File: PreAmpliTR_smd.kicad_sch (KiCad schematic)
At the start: 30 parts, among them J1 Conn_01x02, J2 Conn_01x02, J3 Conn_01x02, Q1 Q_NPN_BEC, Q2 Q_NPN_BEC

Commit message: cambio de valores de los filtros
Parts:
- C3: value 100n -> 680p
- C4: value 100n -> 4700p
- C5: value 1n -> 470p
- C6: value 1n -> 4700p
- R6: value 3K3 -> 100k
- R7: value 3K3 -> 68k
- R8: value 6K8 -> 100k
- RV2, RV3: value 100K -> 1M
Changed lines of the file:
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@@
   (symbol (lib_id "Device:R") (at 123.825 108.585 90) (unit 1)
     (in_bom yes) (on_board yes) (dnp no) (fields_autoplaced)
-    (property "Reference" "R7" (at 123.825 103.505 90)
-      (effects (font (size 1.27 1.27)))
-    )
-    (property "Value" "3K3" (at 123.825 106.045 90)
+    (property "Reference" "R7" (at 123.825 104.14 90)
+      (effects (font (size 1.27 1.27)))
+    )
+    (property "Value" "68k" (at 123.825 106.68 90)
       (effects (font (size 1.27 1.27)))
     )
@@
   (symbol (lib_id "Device:C") (at 92.075 154.305 270) (unit 1)
     (in_bom yes) (on_board yes) (dnp no) (fields_autoplaced)
-    (property "Reference" "C5" (at 92.075 147.955 90)
-      (effects (font (size 1.27 1.27)))
-    )
-    (property "Value" "1n" (at 92.075 150.495 90)
+    (property "Reference" "C5" (at 92.075 148.59 90)
+      (effects (font (size 1.27 1.27)))
+    )
+    (property "Value" "470p" (at 92.075 151.13 90)
       (effects (font (size 1.27 1.27)))
     )
@@
   (symbol (lib_id "Device:C") (at 97.155 114.935 180) (unit 1)
     (in_bom yes) (on_board yes) (dnp no) (fields_autoplaced)
-    (property "Reference" "C3" (at 100.965 114.3 0)
+    (property "Reference" "C3" (at 100.33 114.3 0)
       (effects (font (size 1.27 1.27)) (justify right))
     )
-    (property "Value" "100n" (at 100.965 116.84 0)
+    (property "Value" "680p" (at 100.33 116.84 0)
       (effects (font (size 1.27 1.27)) (justify right))
     )
@@
   (symbol (lib_id "Device:R") (at 90.805 108.585 90) (unit 1)
     (in_bom yes) (on_board yes) (dnp no) (fields_autoplaced)
-    (property "Reference" "R6" (at 90.805 103.505 90)
-      (effects (font (size 1.27 1.27)))
-    )
-    (property "Value" "3K3" (at 90.805 106.045 90)
+    (property "Reference" "R6" (at 90.805 104.14 90)
+      (effects (font (size 1.27 1.27)))
+    )
+    (property "Value" "100k" (at 90.805 106.68 90)
       (effects (font (size 1.27 1.27)))
     )
@@
       (effects (font (size 1.27 1.27)))
     )
-    (property "Value" "100K" (at 107.315 106.045 90)
+    (property "Value" "1M" (at 107.315 106.045 90)
       (effects (font (size 1.27 1.27)))
     )
@@
   (symbol (lib_id "Device:R") (at 107.315 127.635 180) (unit 1)
     (in_bom yes) (on_board yes) (dnp no) (fields_autoplaced)
-    (property "Reference" "R8" (at 109.855 127 0)
+    (property "Reference" "R8" (at 109.22 127 0)
       (effects (font (size 1.27 1.27)) (justify right))
     )
-    (property "Value" "6K8" (at 109.855 129.54 0)
+    (property "Value" "100k" (at 109.22 129.54 0)
       (effects (font (size 1.27 1.27)) (justify right))
     )
@@
       (effects (font (size 1.27 1.27)))
     )
-    (property "Value" "100K" (at 107.315 156.845 90)
+    (property "Value" "1M" (at 107.315 156.845 90)
       (effects (font (size 1.27 1.27)))
     )
@@
   (symbol (lib_id "Device:C") (at 117.475 116.205 180) (unit 1)
     (in_bom yes) (on_board yes) (dnp no) (fields_autoplaced)
-    (property "Reference" "C4" (at 121.285 115.57 0)
+    (property "Reference" "C4" (at 120.65 115.57 0)
       (effects (font (size 1.27 1.27)) (justify right))
     )
-    (property "Value" "100n" (at 121.285 118.11 0)
+    (property "Value" "4700p" (at 120.65 118.11 0)
       (effects (font (size 1.27 1.27)) (justify right))
     )
@@
   (symbol (lib_id "Device:C") (at 121.285 154.305 270) (unit 1)
     (in_bom yes) (on_board yes) (dnp no) (fields_autoplaced)
-    (property "Reference" "C6" (at 121.285 147.955 90)
-      (effects (font (size 1.27 1.27)))
-    )
-    (property "Value" "1n" (at 121.285 150.495 90)
-      (effects (font (size 1.27 1.27)))
-    )
+    (property "Reference" "C6" (at 121.285 148.59 90)
+      (effects (font (size 1.27 1.27)))
+    )
+    (property "Value" "4700p" (at 121.285 151.13 90)
+      (effects (font (size 1.27 1.27)))
+    )

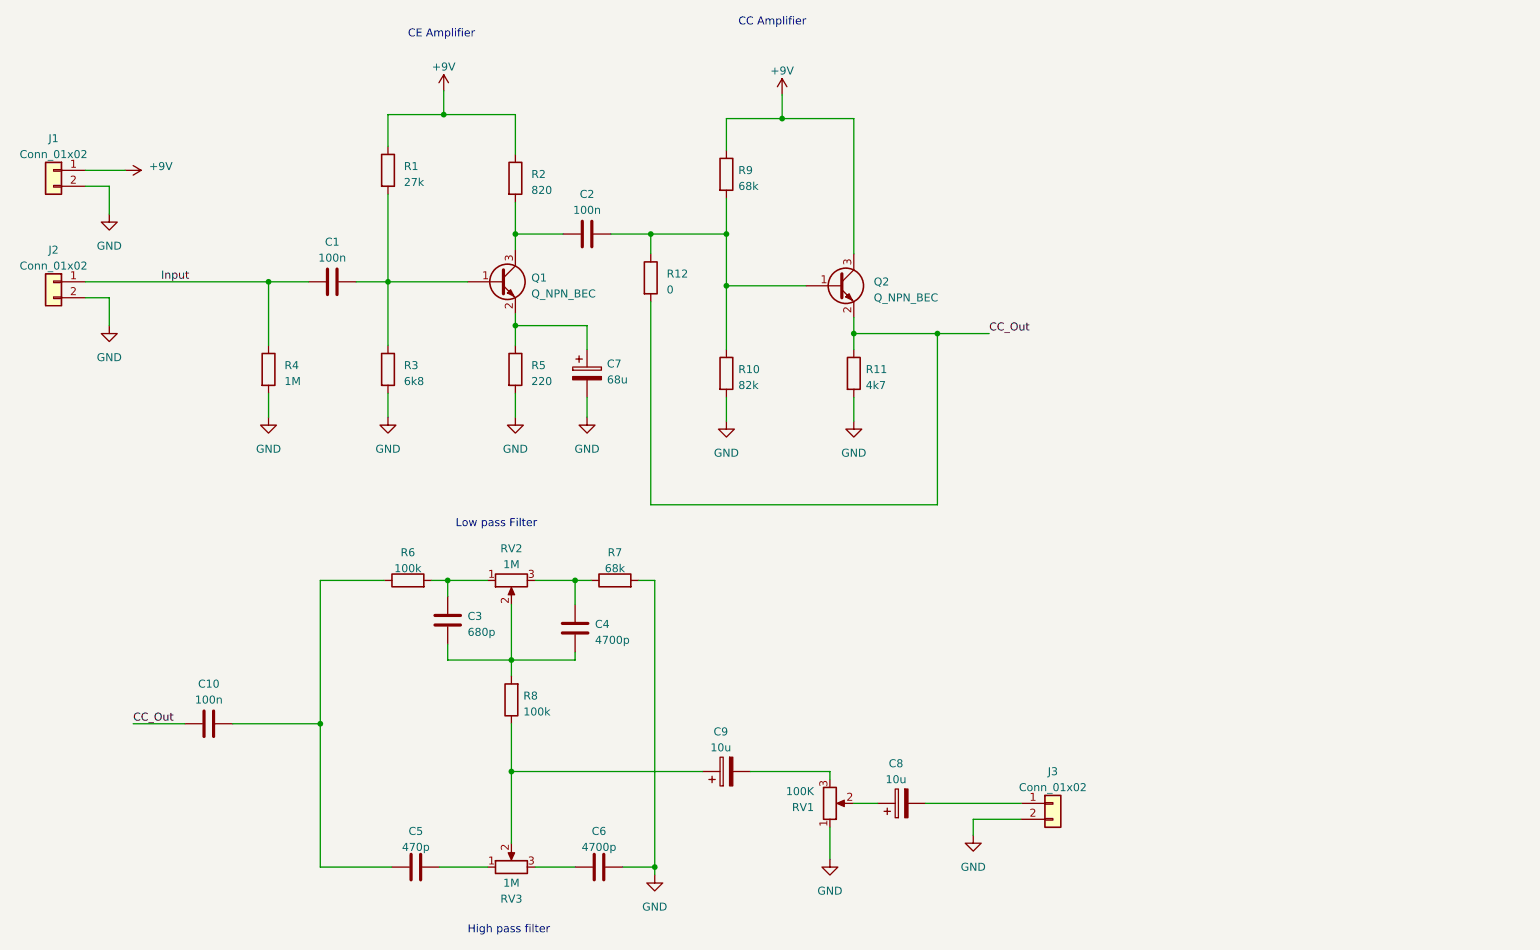
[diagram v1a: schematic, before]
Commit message: cambio de bloques: ec - filtro - cc - salida
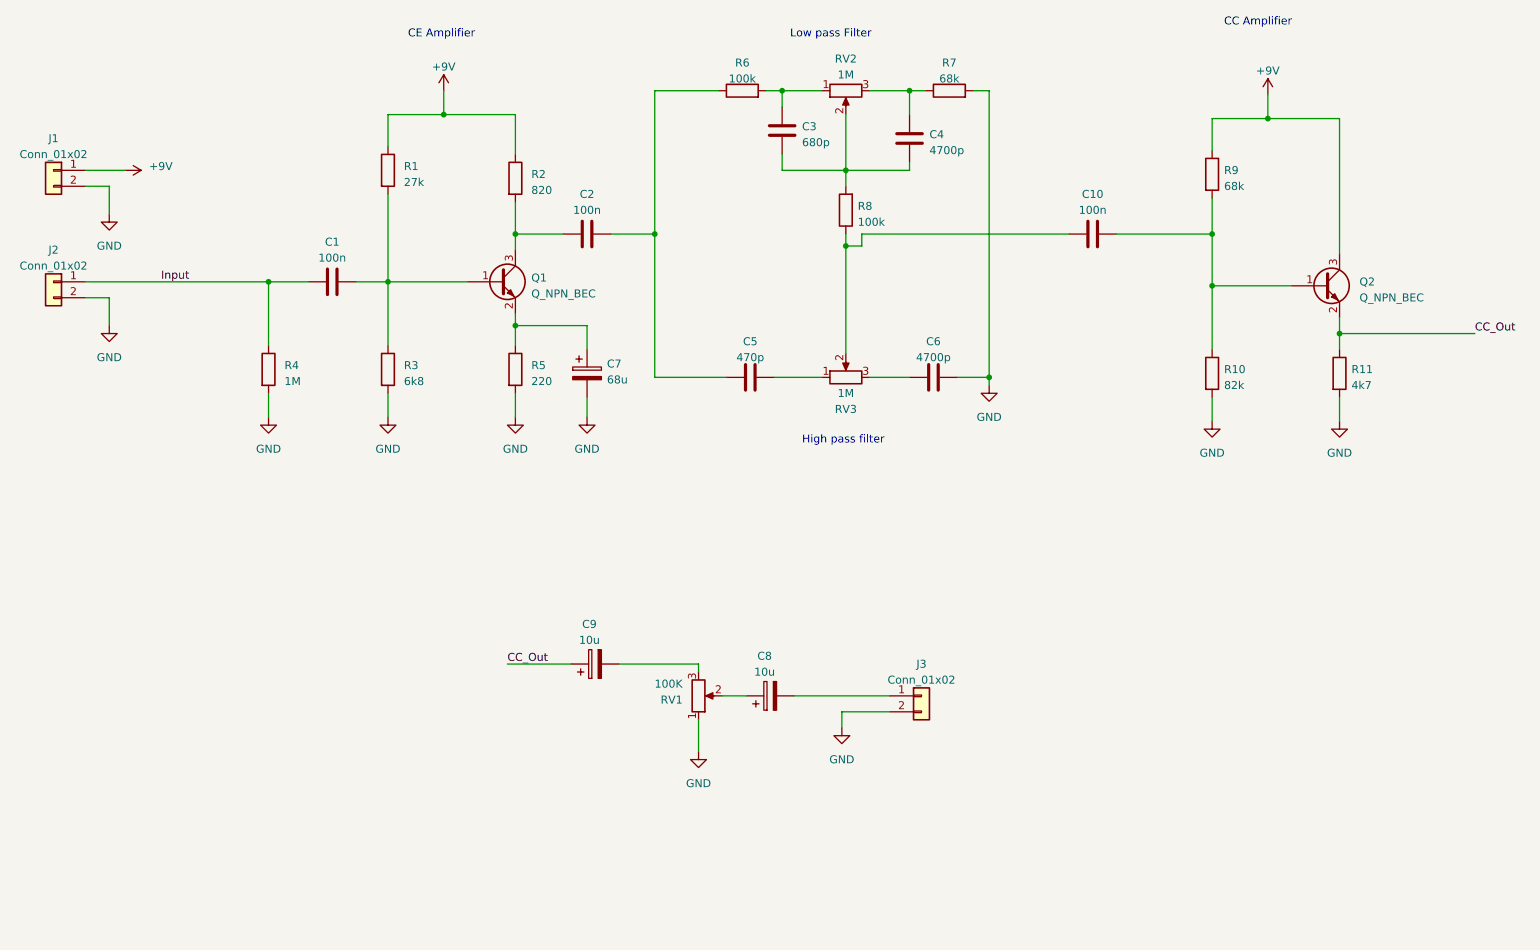
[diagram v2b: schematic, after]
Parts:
- removed R12: 0, Resistor_SMD:R_0805_2012Metric_Pad1.20x1.40mm_HandSolder, symbol Device:R
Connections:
- net CC_Out: now also C9.1; no longer C10.1
- net at Q2.1 (B), R10.1, R9.2: now also C10.2; no longer C2.2
- net at C5.2, R6.1: now also C2.2; no longer C10.2
- net at R8.1, RV3.2: now also C10.1; no longer C9.1
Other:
- moved on the sheet: C10, C3, C4, C5, C6, C8, C9, J3, Q2, R10, R11, R6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
